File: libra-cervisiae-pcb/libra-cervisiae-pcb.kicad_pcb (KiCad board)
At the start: 2 copper layers, 63.8 x 43.2 mm, 159 parts, among them CN1 CP2102, CN3 HX711_BREAKOUT, J1 Board Temp, J10 Load Cell, J12 Load Cell, J4 Wort Temp, J8 Load Cell, J9 Load Cell, SW1 Reset, SW2 Flash, U1 VREG, U2 ESP-12F

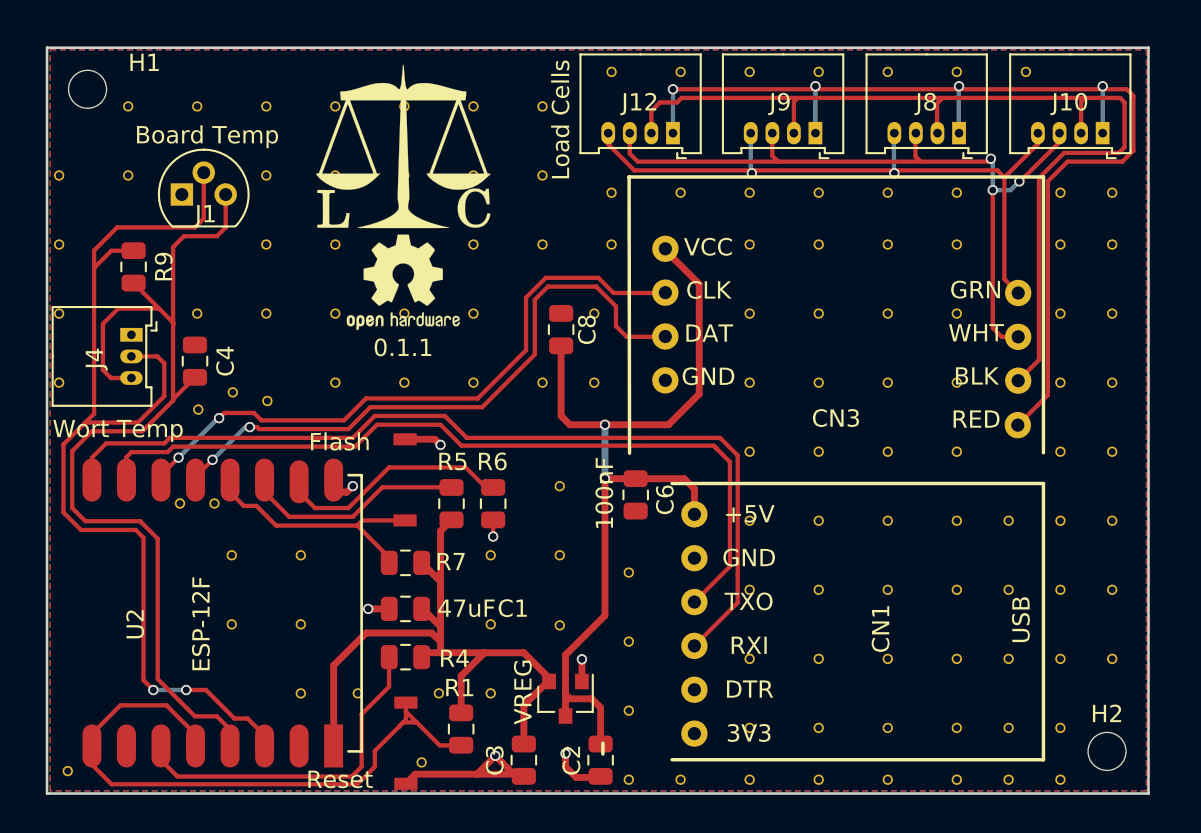
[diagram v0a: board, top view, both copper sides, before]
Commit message: Renumber parts to hit actual number of parts on board
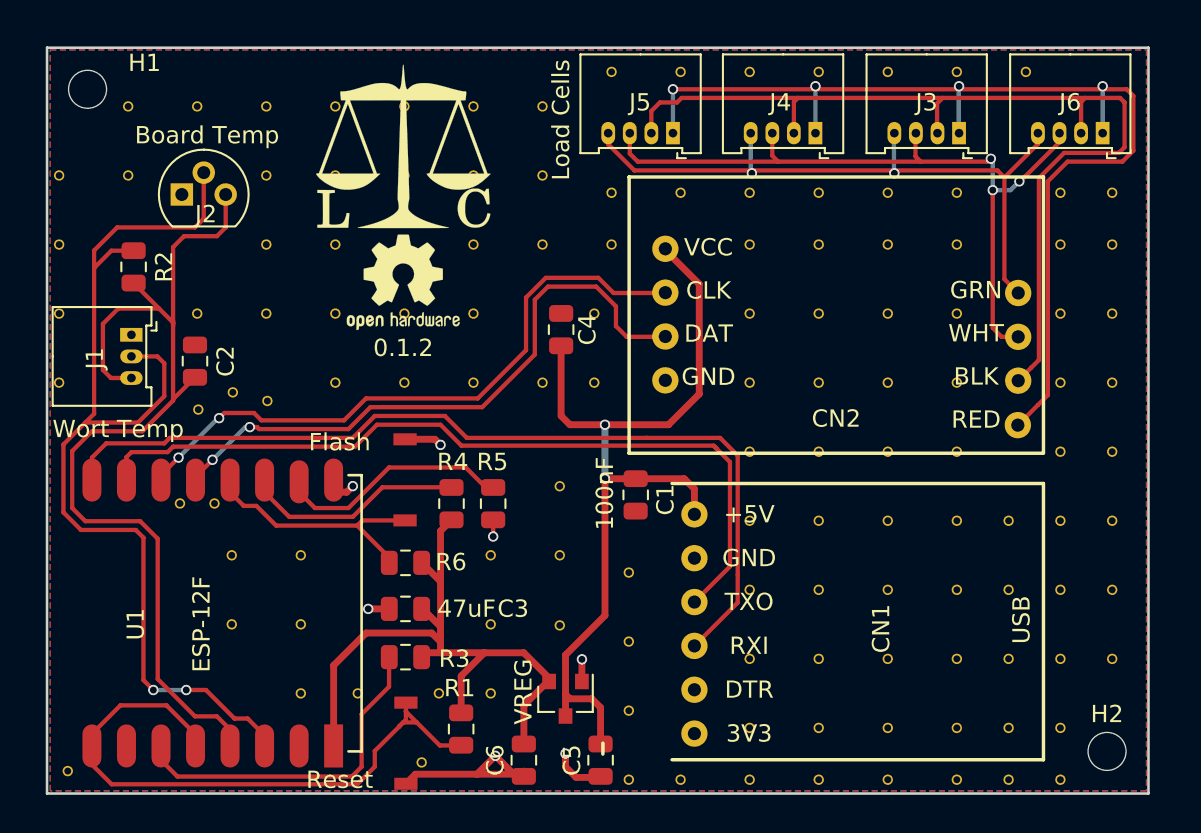
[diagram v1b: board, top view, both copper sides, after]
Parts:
- CN1: value CP2102 -> CP2102-BREAKOUT
- renumbered C6 to C1, C4 to C2, C1 to C3, C8 to C4, C2 to C5, C3 to C6, CN3 to CN2, J4 to J1, J1 to J2, J8 to J3, J9 to J4, J12 to J5, J10 to J6, R9 to R2, R4 to R3, R5 to R4, R6 to R5, R7 to R6, U2 to U1, U1 to U2
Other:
- board text added: "0.1.2"
- board text removed: "0.1.1"

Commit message: Separate S- and E- planes for load cells, more bypass caps
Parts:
- removed the REF** at (131.9, 102.9)
- removed the REF** at (167.9, 76.9)
- removed the REF** at (158.9, 88.9)
- removed the REF** at (138.9, 73.9)
- removed the REF** at (142.9, 73.9)
- removed the REF** at (164.9, 88.9)
- removed the REF** at (164.9, 84.9)
- removed the REF** at (164.9, 80.9)
- removed the REF** at (164.9, 73.9)
- removed the REF** at (164.9, 76.9)
- removed the REF** at (158.9, 76.9)
- removed the REF** at (158.9, 80.9)
- removed the REF** at (158.9, 84.9)
- removed the REF** at (158.9, 73.9)
- removed the REF** at (154.9, 73.9)
- removed the REF** at (150.9, 73.9)
- removed the REF** at (146.9, 73.9)
- removed the REF** at (110.9, 68.9)
- removed the REF** at (137.9, 80.9)
- removed the REF** at (138.9, 66.9)
- removed the REF** at (167.9, 88.9)
- removed the REF** at (167.9, 84.9)
- removed the REF** at (167.9, 80.9)
- removed the REF** at (167.9, 73.9)
- removed the REF** at (162.9, 66.9)
- removed the REF** at (158.9, 66.9)
- removed the REF** at (154.9, 66.9)
- removed the REF** at (150.9, 66.9)
- removed the REF** at (146.9, 66.9)
- removed the REF** at (142.9, 66.9)
- removed the REF** at (128.9, 102.9)
- added C4: .1uF, Capacitor_SMD:C_0805_2012Metric, F.Cu at (127.0, 100.9)
- added C5: .1uF, Capacitor_SMD:C_0805_2012Metric, F.Cu at (138.6, 81.9)
- added REF**: Stitch, Extra_Pads:Stitching_Via_0.6mm, F.Cu at (137.3, 81.0)
- C1: value 100nF -> .1uF
- moved R3 3.78 mm to (129.9, 103.3), turned to 90 degrees
- moved R1 2.46 mm to (132.0, 103.3)
- renumbered C4 to C6, C5 to C7, C6 to C8
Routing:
- net /E-: track 54.6 -> 0.00 mm
- net /S-: track 44.5 -> 0.90 mm, vias 3 -> 0
- net /E+: track 60.2 -> 54.2 mm, vias 4 -> 0
- net /USB+: track 51.5 -> 55.8 mm
- net Net-(R3-Pad1): track 20.8 -> 24.1 mm
- net /S+: track 41.4 -> 38.6 mm, vias 2 -> 0
- net /RST: track 36.0 -> 38.6 mm
- net /3.3+: track 38.4 -> 39.9 mm
- net /GND: track 21.0 -> 22.1 mm, vias 7 -> 8
- added copper zone on B.Cu, net /E-
- added copper zone on F.Cu, net /S-
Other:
- board text added: "0.2.0"
- board text removed: "0.1.2"

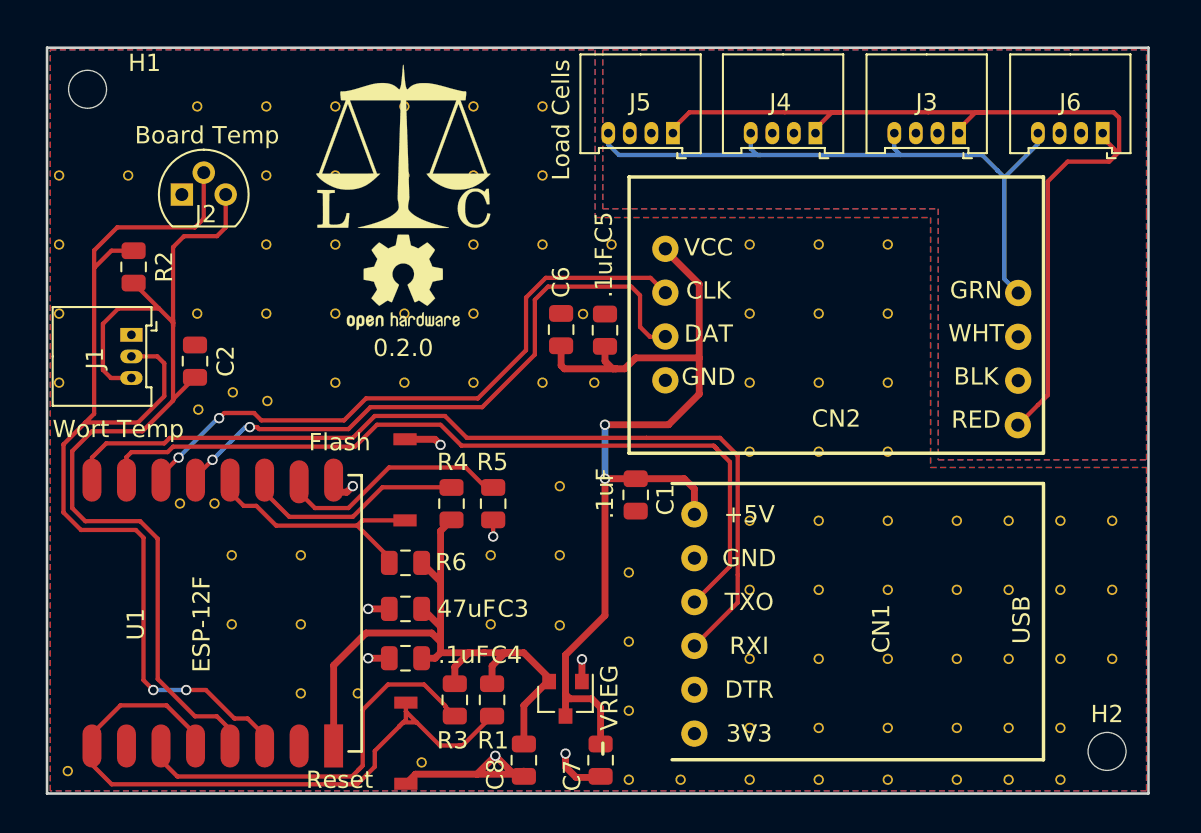
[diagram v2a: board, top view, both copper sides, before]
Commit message: Switch to pin headers/dupont connectors
The wee JST things I bought are next to impossible to do without
specialized tools.
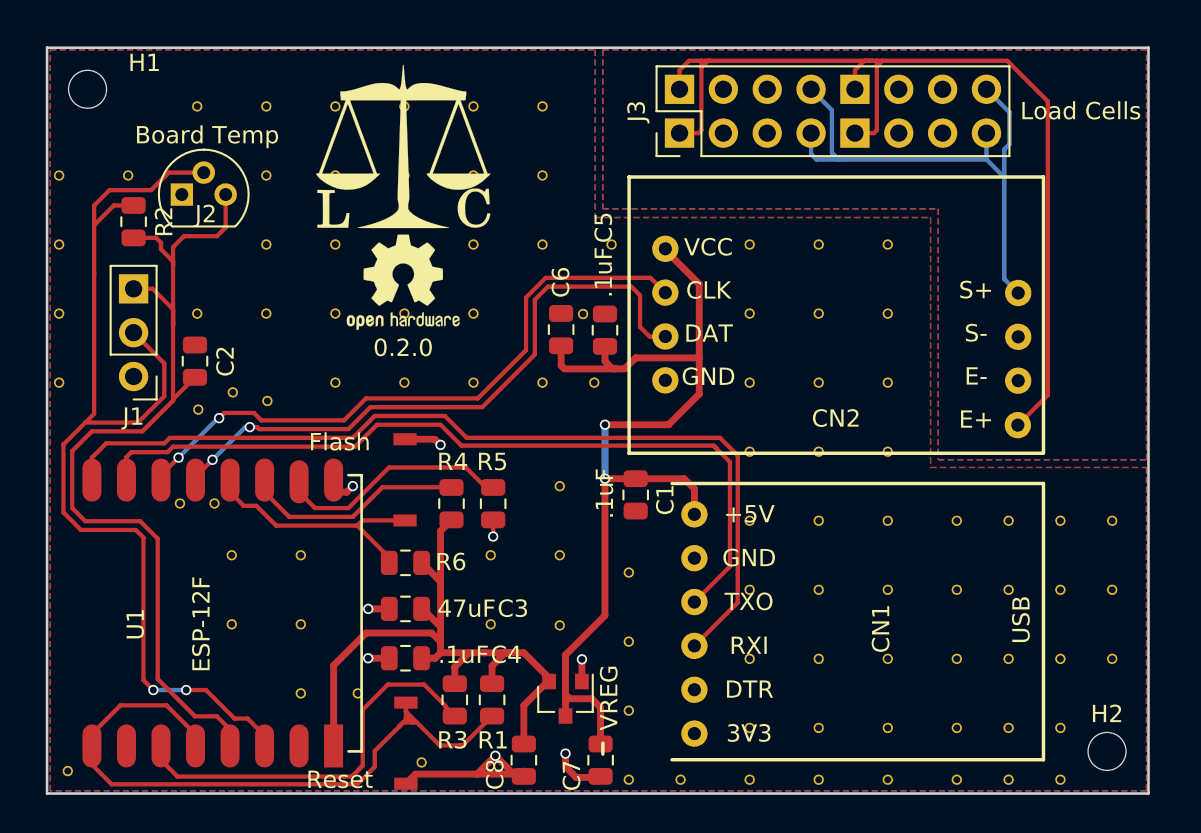
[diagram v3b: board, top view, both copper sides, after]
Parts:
- removed J4, J5, J6: Load Cell, Connector_Molex:Molex_PicoBlade_53048-0810_1x04_P1.25mm_Horizontal
- J1: footprint Connector_Molex:Molex_PicoBlade_53048-0610_1x03_P1.25mm_Horizontal -> Connector_PinHeader_2.54mm:PinHeader_1x03_P2.54mm_Vertical
- J3: value Load Cell -> Load Cells; footprint Connector_Molex:Molex_PicoBlade_53048-0810_1x04_P1.25mm_Horizontal -> Connector_PinHeader_2.54mm:PinHeader_2x08_P2.54mm_Vertical
- moved J3 16.2 mm to (142.9, 70.5), turned to 90 degrees
- moved R2 2.62 mm to (111.3, 75.6)
- moved J1 2.42 mm to (111.3, 84.6), turned to 180 degrees
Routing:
- net /S+: track 38.6 -> 32.1 mm
- net /DS+: track 57.8 -> 53.2 mm
- net /E+: track 54.2 -> 57.3 mm
- net /S-: track 0.90 -> 0.00 mm
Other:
- board text removed: "GRN/WHT +/-S BLK/RED -/+E"

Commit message: PCB 0.2.0 release
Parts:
- removed the REF** at (117.0, 85.5)
- removed the REF** at (114.9, 80.9)
- removed the REF** at (118.9, 80.9)
- added REF**: Stitch, Extra_Pads:Stitching_Via_0.6mm, F.Cu at (111.0, 76.0)
- added REF**: Stitch, Extra_Pads:Stitching_Via_0.6mm, F.Cu at (114.9, 76.0)
- added REF**: Stitch, Extra_Pads:Stitching_Via_0.6mm, F.Cu at (114.9, 73.0)
- added REF**: Stitch, Extra_Pads:Stitching_Via_0.6mm, F.Cu at (110.0, 87.3)
- added REF**: Stitch, Extra_Pads:Stitching_Via_0.6mm, F.Cu at (116.0, 81.0)
- J2: value Board Temp -> Ambient Temp; footprint Package_TO_SOT_THT:TO-92 -> Connector_PinHeader_2.54mm:PinHeader_1x03_P2.54mm_Vertical
- R2: value 10k -> 2.2k
- moved J2 10.2 mm to (113.8, 84.2), turned to 180 degrees
- moved R2 9.55 mm to (118.4, 81.9), turned to 90 degrees
- moved C2 9.01 mm to (112.7, 74.9)
- moved REF** 0.87 mm to (114.7, 87.3)
- moved J1 0.38 mm to (111.3, 84.2)
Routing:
- net /DSD: track 60.8 -> 39.2 mm
- net /DS+: track 53.2 -> 52.2 mm, vias 0 -> 2
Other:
- board text added: "DS+"
- board text added: "DSD"
- board text added: "E+"
- board text added: "E-"
- board text added: "GND"
- board text added: "S+"
- board text added: "S-"
